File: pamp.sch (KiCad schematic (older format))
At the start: 21 parts, among them U1 LM1875

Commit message: Version 1.0b
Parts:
- C3: renamed from C1; footprint Capacitor_THT:C_Disc_D3.4mm_W2.1mm_P2.50mm -> Capacitor_THT:C_Disc_D3.8mm_W2.6mm_P2.50mm
- renumbered C2 to C1, C6 to C2, C7 to C4, C3 to C5, C4 to C6, C8 to C7, C5 to C8, R3 to R1, R6 to R2, R1 to R3, R7 to R5, R8 to R6, R2 to R7, R5 to R8
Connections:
- net spkhot: now also D1.2 (A), D2.1 (K)
- net at C4.1, C5.2, L1.1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: no longer D1.2 (A), D2.1 (K)
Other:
- moved on the sheet: D1, D2
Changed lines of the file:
@@
 $EndDescr
 $Comp
-L Device:C C4
+L Device:C C6
 U 1 1 5ABAB1B4
 P 9900 4250
-F 0 "C4" H 9925 4350 50  0000 L CNN
+F 0 "C6" H 9925 4350 50  0000 L CNN
 F 1 "100n" H 9925 4150 50  0000 L CNN
 F 2 "Capacitor_THT:C_Rect_L7.0mm_W3.5mm_P5.00mm" H 9938 4100 50  0001 C CNN
@@
 $EndComp
 $Comp
-L Device:CP1 C5
+L Device:CP1 C8
 U 1 1 5ABAB333
 P 10200 4250
-F 0 "C5" H 10225 4350 50  0000 L CNN
+F 0 "C8" H 10225 4350 50  0000 L CNN
 F 1 "100u" H 10225 4150 50  0000 L CNN
 F 2 "Capacitor_THT:CP_Radial_D8.0mm_P3.50mm" H 10200 4250 50  0001 C CNN
@@
 $EndComp
 $Comp
-L power:VCC #PWR06
+L power:VCC #PWR08
 U 1 1 5ABAB51E
 P 9900 3900
-F 0 "#PWR06" H 9900 3750 50  0001 C CNN
+F 0 "#PWR08" H 9900 3750 50  0001 C CNN
 F 1 "VCC" H 9900 4050 50  0000 C CNN
 F 2 "" H 9900 3900 50  0001 C CNN
@@
 $EndComp
 $Comp
-L power:VEE #PWR010
+L power:VEE #PWR09
 U 1 1 5ABAB544
 P 9900 5900
-F 0 "#PWR010" H 9900 5750 50  0001 C CNN
+F 0 "#PWR09" H 9900 5750 50  0001 C CNN
 F 1 "VEE" H 9900 6050 50  0000 C CNN
 F 2 "" H 9900 5900 50  0001 C CNN
@@
 Connection ~ 9900 5800
 $Comp
-L power:VCC #PWR05
+L power:VCC #PWR03
 U 1 1 5ABABEED
 P 4800 3700
-F 0 "#PWR05" H 4800 3550 50  0001 C CNN
+F 0 "#PWR03" H 4800 3550 50  0001 C CNN
 F 1 "VCC" H 4800 3850 50  0000 C CNN
 F 2 "" H 4800 3700 50  0001 C CNN
@@
 $EndComp
 $Comp
-L power:VEE #PWR07
+L power:VEE #PWR04
 U 1 1 5ABAC04C
 P 4800 4500
-F 0 "#PWR07" H 4800 4350 50  0001 C CNN
+F 0 "#PWR04" H 4800 4350 50  0001 C CNN
 F 1 "VEE" H 4800 4650 50  0000 C CNN
 F 2 "" H 4800 4500 50  0001 C CNN
@@
 P 10300 4900
 AR Path="/5ABAC584" Ref="#PWR?"  Part="1"
-AR Path="/5ABAAF3C/5ABAC584" Ref="#PWR09"  Part="1"
-F 0 "#PWR09" H 10300 4700 50  0001 C CNN
+AR Path="/5ABAAF3C/5ABAC584" Ref="#PWR010"  Part="1"
+F 0 "#PWR010" H 10300 4700 50  0001 C CNN
 F 1 "GNDPWR" H 10300 4770 50  0000 C CNN
 F 2 "" H 10300 4850 50  0001 C CNN
@@
 Wire Wire Line
 	4700 5000 4800 5000
-Connection ~ 5200 4100
 $Comp
 L power:GNDPWR #PWR?
@@
 P 6100 3150
 AR Path="/5ABAD102" Ref="#PWR?"  Part="1"
-AR Path="/5ABAAF3C/5ABAD102" Ref="#PWR03"  Part="1"
-F 0 "#PWR03" H 6100 2950 50  0001 C CNN
+AR Path="/5ABAAF3C/5ABAD102" Ref="#PWR05"  Part="1"
+F 0 "#PWR05" H 6100 2950 50  0001 C CNN
 F 1 "GNDPWR" H 6100 3020 50  0000 C CNN
 F 2 "" H 6100 3100 50  0001 C CNN
@@
 $EndComp
 $Comp
-L Device:R R5
+L Device:R R8
 U 1 1 5ABAD520
 P 6350 4100
-F 0 "R5" V 6430 4100 50  0000 C CNN
+F 0 "R8" V 6430 4100 50  0000 C CNN
 F 1 "4.7" V 6350 4100 50  0000 C CNN
 F 2 "Resistor_THT:R_Axial_DIN0411_L9.9mm_D3.6mm_P15.24mm_Horizontal" V 6280 4100 50  0001 C CNN
@@
 	6100 4400 6200 4400
 $Comp
-L Device:R R2
+L Device:R R7
 U 1 1 5ABADAC1
 P 6100 3450
-F 0 "R2" V 6180 3450 50  0000 C CNN
+F 0 "R7" V 6180 3450 50  0000 C CNN
 F 1 "4.7" V 6100 3450 50  0000 C CNN
 F 2 "Resistor_THT:R_Axial_DIN0411_L9.9mm_D3.6mm_P15.24mm_Horizontal" V 6030 3450 50  0001 C CNN
@@
 Wire Wire Line
 	6100 3300 6100 3150
-Text HLabel 7000 4100 2    60   Output ~ 0
+Text HLabel 7200 4100 2    60   Output ~ 0
 spkhot
 $Comp
-L power:VCC #PWR04
+L power:VCC #PWR06
 U 1 1 5ABAF917
-P 5500 3600
-F 0 "#PWR04" H 5500 3450 50  0001 C CNN
-F 1 "VCC" H 5500 3750 50  0000 C CNN
-F 2 "" H 5500 3600 50  0001 C CNN
-F 3 "" H 5500 3600 50  0001 C CNN
-	1    5500 3600
-	1    0    0    -1
-$EndComp
-$Comp
-L power:VEE #PWR08
+P 6900 3600
+F 0 "#PWR06" H 6900 3450 50  0001 C CNN
+F 1 "VCC" H 6900 3750 50  0000 C CNN
+F 2 "" H 6900 3600 50  0001 C CNN
+F 3 "" H 6900 3600 50  0001 C CNN
+	1    6900 3600
+	1    0    0    -1
+$EndComp
+$Comp
+L power:VEE #PWR07
 U 1 1 5ABAF97F
-P 5500 4600
-F 0 "#PWR08" H 5500 4450 50  0001 C CNN
-F 1 "VEE" H 5500 4750 50  0000 C CNN
-F 2 "" H 5500 4600 50  0001 C CNN
-F 3 "" H 5500 4600 50  0001 C CNN
-	1    5500 4600
+P 6900 4600
+F 0 "#PWR07" H 6900 4450 50  0001 C CNN
+F 1 "VEE" H 6900 4750 50  0000 C CNN
+F 2 "" H 6900 4600 50  0001 C CNN
+F 3 "" H 6900 4600 50  0001 C CNN
+	1    6900 4600
 	-1   0    0    1
 $EndComp
 Wire Wire Line
-	5500 4500 5500 4600
-Wire Wire Line
-	5500 3700 5500 3600
-$Comp
-L Device:CP1 C2
+	6900 4500 6900 4600
+Wire Wire Line
+	6900 3700 6900 3600
+$Comp
+L Device:CP1 C1
 U 1 1 5ABAFDD9
 P 3650 3500
-F 0 "C2" H 3675 3600 50  0000 L CNN
+F 0 "C1" H 3675 3600 50  0000 L CNN
 F 1 "470u" H 3675 3400 50  0000 L CNN
 F 2 "Capacitor_THT:CP_Radial_D8.0mm_P3.50mm" H 3650 3500 50  0001 C CNN
@@
 L Diode:1N5404 D2
 U 1 1 5AC0CCC8
-P 5500 4350
-F 0 "D2" H 5500 4450 50  0000 C CNN
-F 1 "1N5404" H 5500 4250 50  0000 C CNN
-F 2 "Diode_THT:D_DO-201AD_P12.70mm_Horizontal" H 5500 4175 50  0001 C CNN
-F 3 "" H 5500 4350 50  0001 C CNN
-	1    5500 4350
-	0    1    1    0
-$EndComp
-$Comp
-L Device:R R8
+P 6900 4350
+F 0 "D2" H 6900 4450 50  0000 C CNN
+F 1 "1N5404" H 6900 4250 50  0000 C CNN
+F 2 "Diode_THT:D_DO-201AD_P12.70mm_Horizontal" H 6900 4175 50  0001 C CNN
+F 3 "" H 6900 4350 50  0001 C CNN
+	1    6900 4350
+	0    1    1    0
+$EndComp
+$Comp
+L Device:R R6
 U 1 1 5AC10204
 P 4550 5000
-F 0 "R8" V 4630 5000 50  0000 C CNN
+F 0 "R6" V 4630 5000 50  0000 C CNN
 F 1 "1k6" V 4550 5000 50  0000 C CNN
 F 2 "Resistor_THT:R_Axial_DIN0207_L6.3mm_D2.5mm_P10.16mm_Horizontal" V 4480 5000 50  0001 C CNN
@@
 	4300 4200 4500 4200
 $Comp
-L Device:C C7
+L Device:C C4
 U 1 1 5AC80639
 P 4950 5000
-F 0 "C7" H 4975 5100 50  0000 L CNN
+F 0 "C4" H 4975 5100 50  0000 L CNN
 F 1 "15p" H 4975 4900 50  0000 L CNN
 F 2 "Capacitor_THT:C_Disc_D3.8mm_W2.6mm_P2.50mm" H 4988 4850 50  0001 C CNN
@@
 $EndComp
 $Comp
-L Device:C C8
+L Device:C C7
 U 1 1 5AC8C9A2
 P 9900 5150
-F 0 "C8" H 9925 5250 50  0000 L CNN
+F 0 "C7" H 9925 5250 50  0000 L CNN
 F 1 "100n" H 9925 5050 50  0000 L CNN
 F 2 "Capacitor_THT:C_Rect_L7.0mm_W3.5mm_P5.00mm" H 9938 5000 50  0001 C CNN
@@
 $EndComp
 $Comp
-L Device:C C3
+L Device:C C5
 U 1 1 5AC8DC6B
 P 6100 3850
-F 0 "C3" H 6125 3950 50  0000 L CNN
+F 0 "C5" H 6125 3950 50  0000 L CNN
 F 1 "220n" H 6125 3750 50  0000 L CNN
 F 2 "Capacitor_THT:C_Rect_L7.0mm_W3.5mm_P5.00mm" H 6138 3700 50  0001 C CNN
@@
 $EndComp
 $Comp
-L Device:CP1 C6
+L Device:CP1 C2
 U 1 1 5AD5D094
 P 3650 4700
-F 0 "C6" H 3675 4800 50  0000 L CNN
+F 0 "C2" H 3675 4800 50  0000 L CNN
 F 1 "470u" H 3675 4600 50  0000 L CNN
 F 2 "Capacitor_THT:CP_Radial_D8.0mm_P3.50mm" H 3650 4700 50  0001 C CNN
@@
 	4700 4500 4800 4500
 $Comp
-L Device:R R6
+L Device:R R2
 U 1 1 5AD67EF8
 P 4050 4700
-F 0 "R6" V 4130 4700 50  0000 C CNN
+F 0 "R2" V 4130 4700 50  0000 C CNN
 F 1 "499" V 4050 4700 50  0000 C CNN
 F 2 "Resistor_THT:R_Axial_DIN0207_L6.3mm_D2.5mm_P10.16mm_Horizontal" V 3980 4700 50  0001 C CNN
@@
 $EndComp
 $Comp
-L Device:R R7
+L Device:R R5
 U 1 1 5AD68E38
 P 4550 4700
-F 0 "R7" V 4630 4700 50  0000 C CNN
+F 0 "R5" V 4630 4700 50  0000 C CNN
 F 1 "15k" V 4550 4700 50  0000 C CNN
 F 2 "Resistor_THT:R_Axial_DIN0207_L6.3mm_D2.5mm_P10.16mm_Horizontal" V 4480 4700 50  0001 C CNN
@@
 	4700 3200 4800 3200
 $Comp
-L Device:R R1
+L Device:R R3
 U 1 1 5B1A76CE
 P 4550 3200
-F 0 "R1" V 4630 3200 50  0000 C CNN
+F 0 "R3" V 4630 3200 50  0000 C CNN
 F 1 "1k6" V 4550 3200 50  0000 C CNN
 F 2 "Resistor_THT:R_Axial_DIN0207_L6.3mm_D2.5mm_P10.16mm_Horizontal" V 4480 3200 50  0001 C CNN
@@
 $EndComp
 $Comp
-L Device:C C1
+L Device:C C3
 U 1 1 5B1A76D8
 P 4950 3200
-F 0 "C1" H 4975 3300 50  0000 L CNN
+F 0 "C3" H 4975 3300 50  0000 L CNN
 F 1 "15p" H 4975 3100 50  0000 L CNN
-F 2 "Capacitor_THT:C_Disc_D3.4mm_W2.1mm_P2.50mm" H 4988 3050 50  0001 C CNN
+F 2 "Capacitor_THT:C_Disc_D3.8mm_W2.6mm_P2.50mm" H 4988 3050 50  0001 C CNN
 F 3 "http://www.farnell.com/datasheets/1825496.pdf" H 4950 3200 50  0001 C CNN
 F 4 "100V" H 5000 2900 60  0000 L CNN "Voltage"
@@
 	9900 5800 9900 5900
 Wire Wire Line
-	5200 4100 5500 4100
-Wire Wire Line
 	6100 4100 6100 4400
 Wire Wire Line
@@
 	3100 4700 3500 4700
 $Comp
-L Device:R R3
+L Device:R R1
 U 1 1 5B60E4BF
 P 4050 3500
-F 0 "R3" V 4130 3500 50  0000 C CNN
+F 0 "R1" V 4130 3500 50  0000 C CNN
 F 1 "499" V 4050 3500 50  0000 C CNN
 F 2 "Resistor_THT:R_Axial_DIN0207_L6.3mm_D2.5mm_P10.16mm_Horizontal" V 3980 3500 50  0001 C CNN
@@
 sgnd
 Wire Wire Line
-	5500 4000 5500 4100
-Wire Wire Line
-	6600 4100 7000 4100
-Connection ~ 5500 4100
-Wire Wire Line
-	5500 4100 6100 4100
-Wire Wire Line
-	5500 4100 5500 4200
+	6600 4100 6900 4100
 $Comp
 L Amplifier_Audio:LM1875 U1
@@
 L Diode:1N5404 D1
 U 1 1 5AC0C9F9
-P 5500 3850
-F 0 "D1" H 5500 3950 50  0000 C CNN
-F 1 "1N5404" H 5500 3750 50  0000 C CNN
-F 2 "Diode_THT:D_DO-201AD_P12.70mm_Horizontal" H 5500 3675 50  0001 C CNN
-F 3 "" H 5500 3850 50  0001 C CNN
-	1    5500 3850
-	0    1    1    0
-$EndComp
+P 6900 3850
+F 0 "D1" H 6900 3950 50  0000 C CNN
+F 1 "1N5404" H 6900 3750 50  0000 C CNN
+F 2 "Diode_THT:D_DO-201AD_P12.70mm_Horizontal" H 6900 3675 50  0001 C CNN
+F 3 "" H 6900 3850 50  0001 C CNN
+	1    6900 3850
+	0    1    1    0
+$EndComp
+Wire Wire Line
+	6900 4000 6900 4100
+Wire Wire Line
+	5200 4100 6100 4100
+Connection ~ 5200 4100
+Connection ~ 6900 4100
+Wire Wire Line
+	6900 4100 7200 4100
+Wire Wire Line
+	6900 4100 6900 4200
 $EndSCHEMATC

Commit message: Release Version 1.0
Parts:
- C3, C4: Manufacturer Multicomp:MCMT21N150F101CT -> AVX:SR151A150JAR; Vendor Farnel:1856264 -> Farnel:1100498
- C5: Manufacturer Multicomp:MCSH31B224K101CT -> WIMA:MKS2D032201C00KSSD; Type X7R -> PET; Vendor Farnell:1856615 -> Farnell:1890146
- C6, C7: Manufacturer Multicomp:MCSH31B104K101CT -> WIMA:MKP2D031001F00KSSD; Type X7R -> PP; Vendor Farnell:1856606 -> Farnell:1890265
- D1, D2: Manufacturer (none) -> ON Semiconductor:1N5404RL; Vendor (none) -> Farnell:9556141
- R1, R2: Manufacturer PANASONIC:ERA8AEB4990V -> TE Connectivity:LR1F499R; Power 1/4 -> 0.6W; Vendor Farnell:2095153 -> Farnell:2330163
- R3, R6: Manufacturer (none) -> TE Connectivity:LR0204F1K6; Power (none) -> 0.25W; Type (none) -> MF; Vendor (none) -> Farnell:2329892
- R4, R5: value 15k -> 7k5; Manufacturer PANASONIC:ERA8AEB153V -> TE Connectivity:LR1F7K5; Power 1/4 -> 0.6W; Vendor Farnell:1717752 -> Farnell:2330223
- R7, R8: Manufacturer (none) -> Vishay:PR02000204708JA100; Power (none) -> 2W; Type (none) -> MF; Vendor (none) -> Farnell:2614544
- U1: Manufacturer (none) -> TI:LM1875T/NOPB; Vendor (none) -> Farnell:1468913
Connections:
- net spkhot: no longer D1.2 (A), D2.1 (K)
- net at C4.1, C5.2, L1.1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: now also D1.2 (A), D2.1 (K)
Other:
- moved on the sheet: C3, C4, C5, D1, D2, R3, R6, R7

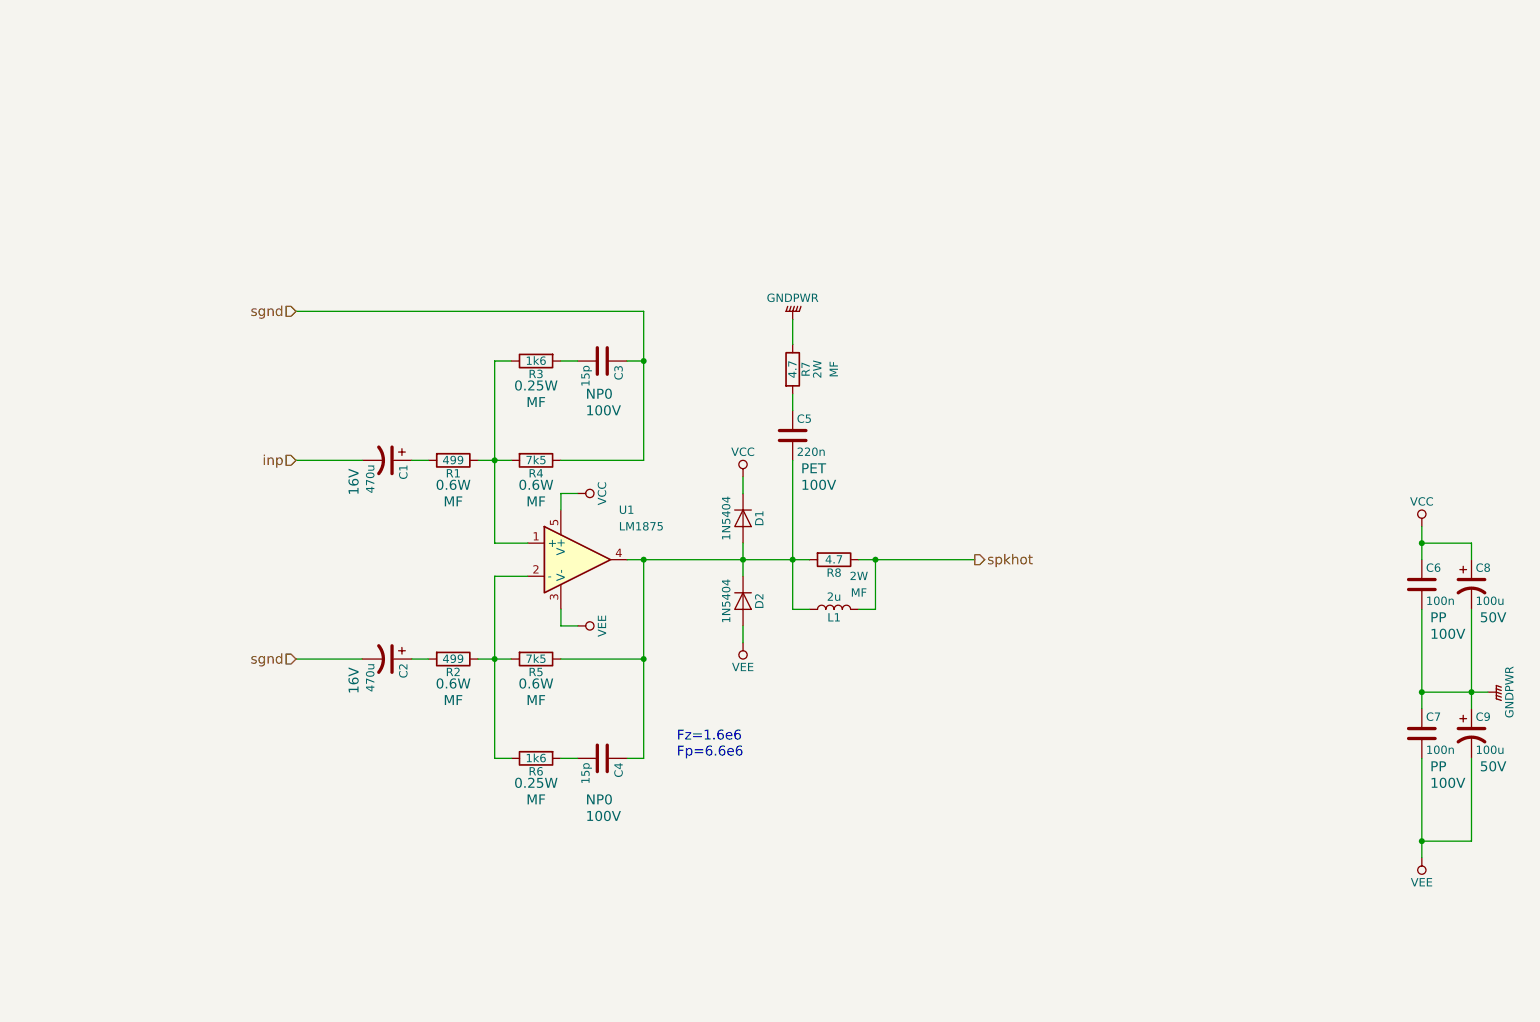
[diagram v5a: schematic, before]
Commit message: Releasing version with distant psu caps.
Signed-off-by: Nenad Radulovic <nenad.b.radulovic@gmail.com>
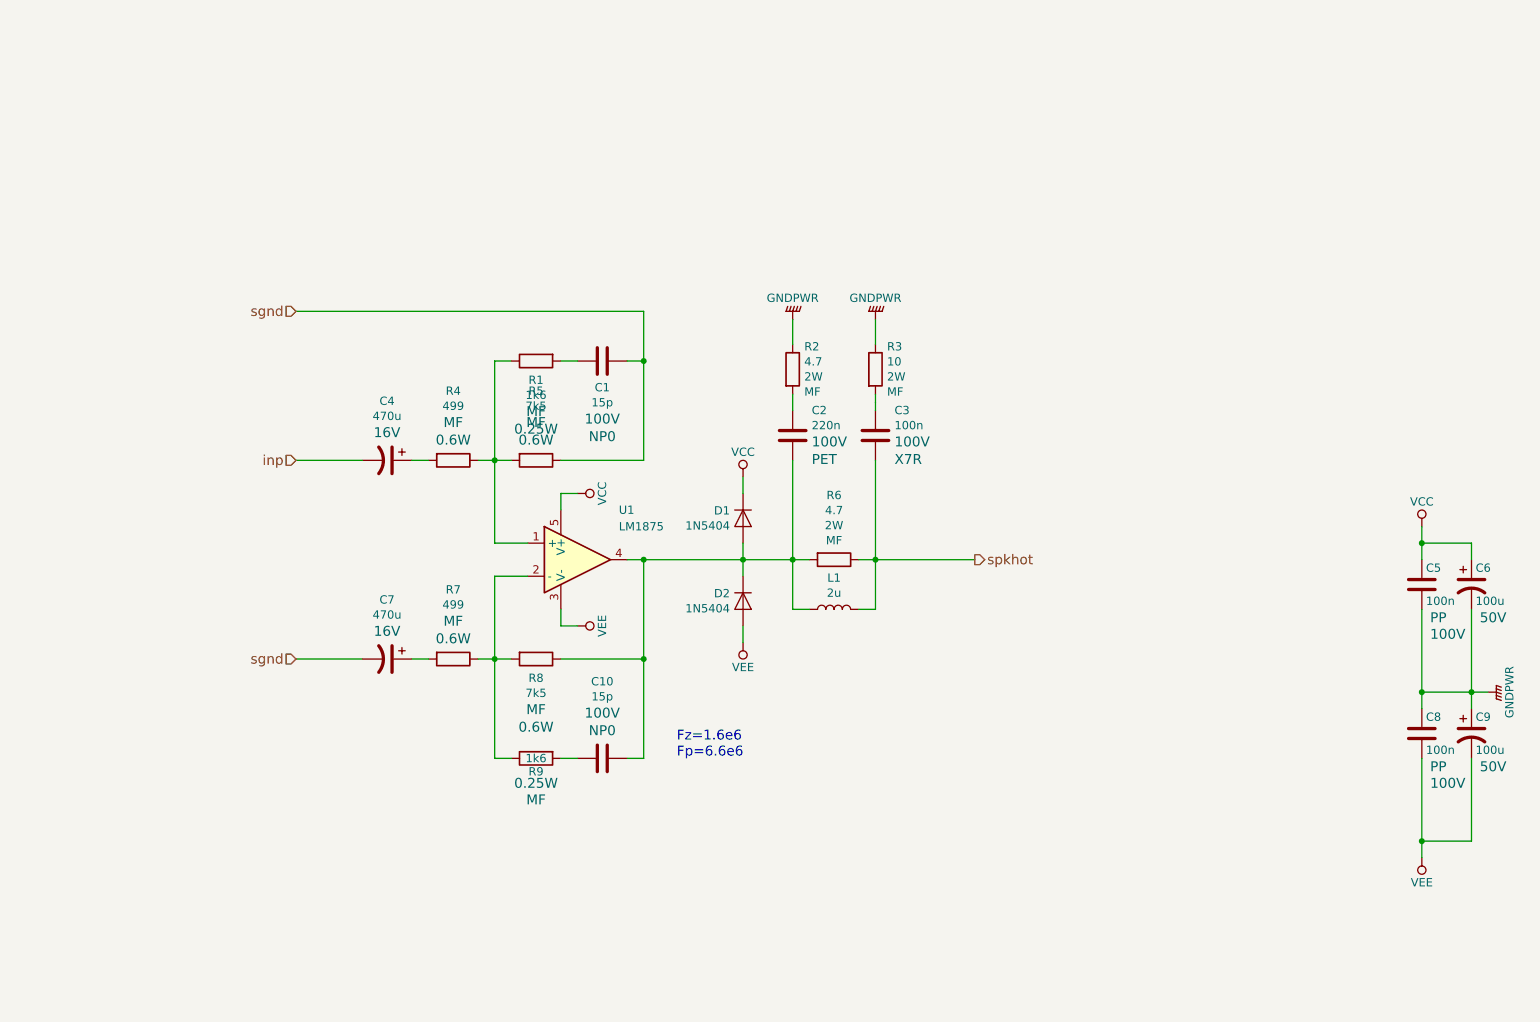
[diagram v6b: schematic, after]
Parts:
- added C3: 100n, Capacitor_THT:C_Disc_D5.1mm_W3.2mm_P5.00mm, symbol Device:C
- added R2: 4.7, Resistor_THT:R_Axial_DIN0411_L9.9mm_D3.6mm_P15.24mm_Horizontal, symbol Device:R
- C1: renamed from C3; footprint Capacitor_THT:C_Disc_D3.8mm_W2.6mm_P2.50mm -> Capacitor_THT:C_Disc_D3.4mm_W2.1mm_P2.50mm
- C10: renamed from C4; footprint Capacitor_THT:C_Disc_D3.8mm_W2.6mm_P2.50mm -> Capacitor_THT:C_Disc_D3.4mm_W2.1mm_P2.50mm
- R3: renamed from R7; value 4.7 -> 10; Manufacturer Vishay:PR02000204708JA100 -> Vishay:PR02000201009JA100; Vendor Farnell:2614544 -> Farnell:2614526
- renumbered C5 to C2, C1 to C4, C6 to C5, C8 to C6, C2 to C7, C7 to C8, R3 to R1, R1 to R4, R4 to R5, R8 to R6, R2 to R7, R5 to R8, R6 to R9
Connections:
- net GNDPWR: now also R2.1
- net spkhot: now also C3.2
- net at R3.2: now also C3.1; no longer C2.1
- new net: C2.1, R2.2
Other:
- moved on the sheet: R3

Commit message: Relase v1.0
Corrected a few things on the PCB.
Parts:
- R1, R9: footprint Resistor_THT:R_Axial_DIN0207_L6.3mm_D2.5mm_P10.16mm_Horizontal -> Resistor_THT:R_Axial_DIN0207_L6.3mm_D2.5mm_P7.62mm_Horizontal
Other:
- note added: "Put R3 and C3 right next to output \nconnector. Also, the return ground \nshould be at the connector side."
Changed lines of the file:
@@
 U 1 1 5ABAB1B4
 P 9900 4250
-F 0 "C5" H 9925 4350 50  0000 L CNN
-F 1 "100n" H 9925 4150 50  0000 L CNN
+F 0 "C5" H 9786 4402 50  0000 R CNN
+F 1 "100n" H 9786 4311 50  0000 R CNN
 F 2 "Capacitor_THT:C_Rect_L7.0mm_W3.5mm_P5.00mm" H 9938 4100 50  0001 C CNN
 F 3 "http://www.farnell.com/datasheets/1784425.pdf" H 9900 4250 50  0001 C CNN
-F 4 "100V" H 9950 3950 60  0000 L CNN "Voltage"
-F 5 "PP" H 9950 4050 60  0000 L CNN "Type"
+F 4 "100V" H 9786 4212 60  0000 R CNN "Voltage"
+F 5 "PP" H 9786 4106 60  0000 R CNN "Type"
 F 6 "Farnell:1890265" H 9900 4250 60  0001 C CNN "Vendor"
 F 7 "WIMA:MKP2D031001F00KSSD" H 9900 4250 60  0001 C CNN "Manufacturer"
@@
 U 1 1 5ABAB333
 P 10200 4250
-F 0 "C6" H 10225 4350 50  0000 L CNN
-F 1 "100u" H 10225 4150 50  0000 L CNN
+F 0 "C6" H 10315 4349 50  0000 L CNN
+F 1 "100u" H 10315 4258 50  0000 L CNN
 F 2 "Capacitor_THT:CP_Radial_D8.0mm_P3.50mm" H 10200 4250 50  0001 C CNN
 F 3 "http://www.farnell.com/datasheets/2321304.pdf" H 10200 4250 50  0001 C CNN
-F 4 "50V" H 10250 4050 60  0000 L CNN "Voltage"
+F 4 "50V" H 10315 4159 60  0000 L CNN "Voltage"
 F 5 "Farnell:2346269" H 10200 4250 60  0001 C CNN "Vendor"
 F 6 "Rybicon:50YXJ100MT78X11.5" H 10200 4250 60  0001 C CNN "Manufacturer"
@@
 U 1 1 5AC10204
 P 4550 5300
-F 0 "R9" V 4630 5300 50  0000 C CNN
-F 1 "1k6" V 4550 5300 50  0000 C CNN
-F 2 "Resistor_THT:R_Axial_DIN0207_L6.3mm_D2.5mm_P10.16mm_Horizontal" V 4480 5300 50  0001 C CNN
+F 0 "R9" V 4665 5300 50  0000 C CNN
+F 1 "1k6" V 4756 5300 50  0000 C CNN
+F 2 "Resistor_THT:R_Axial_DIN0207_L6.3mm_D2.5mm_P7.62mm_Horizontal" V 4480 5300 50  0001 C CNN
 F 3 "http://www.farnell.com/datasheets/1723855.pdf" H 4550 5300 50  0001 C CNN
 F 4 "Farnell:2329892" V 4550 5300 50  0001 C CNN "Vendor"
 F 5 "TE Connectivity:LR0204F1K6" V 4550 5300 50  0001 C CNN "Manufacturer"
-F 6 "0.25W" V 4700 5300 60  0000 C CNN "Power"
-F 7 "MF" V 4800 5300 60  0000 C CNN "Type"
+F 6 "0.25W" V 4855 5300 60  0000 C CNN "Power"
+F 7 "MF" V 4961 5300 60  0000 C CNN "Type"
 	1    4550 5300
 	0    -1   1    0
@@
 U 1 1 5AC8C9A2
 P 9900 5150
-F 0 "C8" H 9925 5250 50  0000 L CNN
-F 1 "100n" H 9925 5050 50  0000 L CNN
+F 0 "C8" H 9786 5302 50  0000 R CNN
+F 1 "100n" H 9786 5211 50  0000 R CNN
 F 2 "Capacitor_THT:C_Rect_L7.0mm_W3.5mm_P5.00mm" H 9938 5000 50  0001 C CNN
 F 3 "http://www.farnell.com/datasheets/1784425.pdf" H 9900 5150 50  0001 C CNN
-F 4 "100V" H 9950 4850 60  0000 L CNN "Voltage"
-F 5 "PP" H 9950 4950 60  0000 L CNN "Type"
+F 4 "100V" H 9786 5112 60  0000 R CNN "Voltage"
+F 5 "PP" H 9786 5006 60  0000 R CNN "Type"
 F 6 "Farnell:1890265" H 9900 5150 60  0001 C CNN "Vendor"
 F 7 "WIMA:MKP2D031001F00KSSD" H 9900 5150 60  0001 C CNN "Manufacturer"
@@
 U 1 1 5ACDCA60
 P 10200 5150
-F 0 "C9" H 10225 5250 50  0000 L CNN
-F 1 "100u" H 10225 5050 50  0000 L CNN
+F 0 "C9" H 10315 5249 50  0000 L CNN
+F 1 "100u" H 10315 5158 50  0000 L CNN
 F 2 "Capacitor_THT:CP_Radial_D8.0mm_P3.50mm" H 10200 5150 50  0001 C CNN
 F 3 "http://www.farnell.com/datasheets/2321304.pdf" H 10200 5150 50  0001 C CNN
-F 4 "50V" H 10250 4950 60  0000 L CNN "Voltage"
+F 4 "50V" H 10315 5059 60  0000 L CNN "Voltage"
 F 5 "Farnell:2346269" H 10200 5150 60  0001 C CNN "Vendor"
 F 6 "Rybicon:50YXJ100MT78X11.5" H 10200 5150 60  0001 C CNN "Manufacturer"
@@
 U 1 1 5B1A76CE
 P 4550 2900
-F 0 "R1" V 4665 2900 50  0000 C CNN
-F 1 "1k6" V 4756 2900 50  0000 C CNN
-F 2 "Resistor_THT:R_Axial_DIN0207_L6.3mm_D2.5mm_P10.16mm_Horizontal" V 4480 2900 50  0001 C CNN
+F 0 "R1" V 4100 2900 50  0000 C CNN
+F 1 "1k6" V 4200 2900 50  0000 C CNN
+F 2 "Resistor_THT:R_Axial_DIN0207_L6.3mm_D2.5mm_P7.62mm_Horizontal" V 4480 2900 50  0001 C CNN
 F 3 "http://www.farnell.com/datasheets/1723855.pdf" H 4550 2900 50  0001 C CNN
 F 4 "TE Connectivity:LR0204F1K6" V 4550 2900 50  0001 C CNN "Manufacturer"
 F 5 "Farnell:2329892" V 4550 2900 50  0001 C CNN "Vendor"
-F 6 "MF" V 4855 2900 60  0000 C CNN "Type"
-F 7 "0.25W" V 4961 2900 60  0000 C CNN "Power"
+F 6 "MF" V 4300 2900 60  0000 C CNN "Type"
+F 7 "0.25W" V 4400 2900 60  0000 C CNN "Power"
 	1    4550 2900
 	0    -1   1    0
@@
 	6600 3500 6600 4100
 Wire Wire Line
-	6600 3200 6600 3150
-Wire Wire Line
 	6600 2800 6600 2650
 $Comp
@@
 $EndComp
 Wire Wire Line
-	6600 3150 6600 3100
+	6600 3100 6600 3200
+Text Notes 7050 3050 0    50   ~ 0
+Put R3 and C3 right next to output \nconnector. Also, the return ground \nshould be at the connector side.
 $EndSCHEMATC
